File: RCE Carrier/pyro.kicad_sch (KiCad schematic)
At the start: 31 parts, among them J1 TBL002A-350-08GY-2GY, Q5 SI7232DN-T1-GE3, Q6 SI7232DN-T1-GE3, U6 LM293, U7 LM293

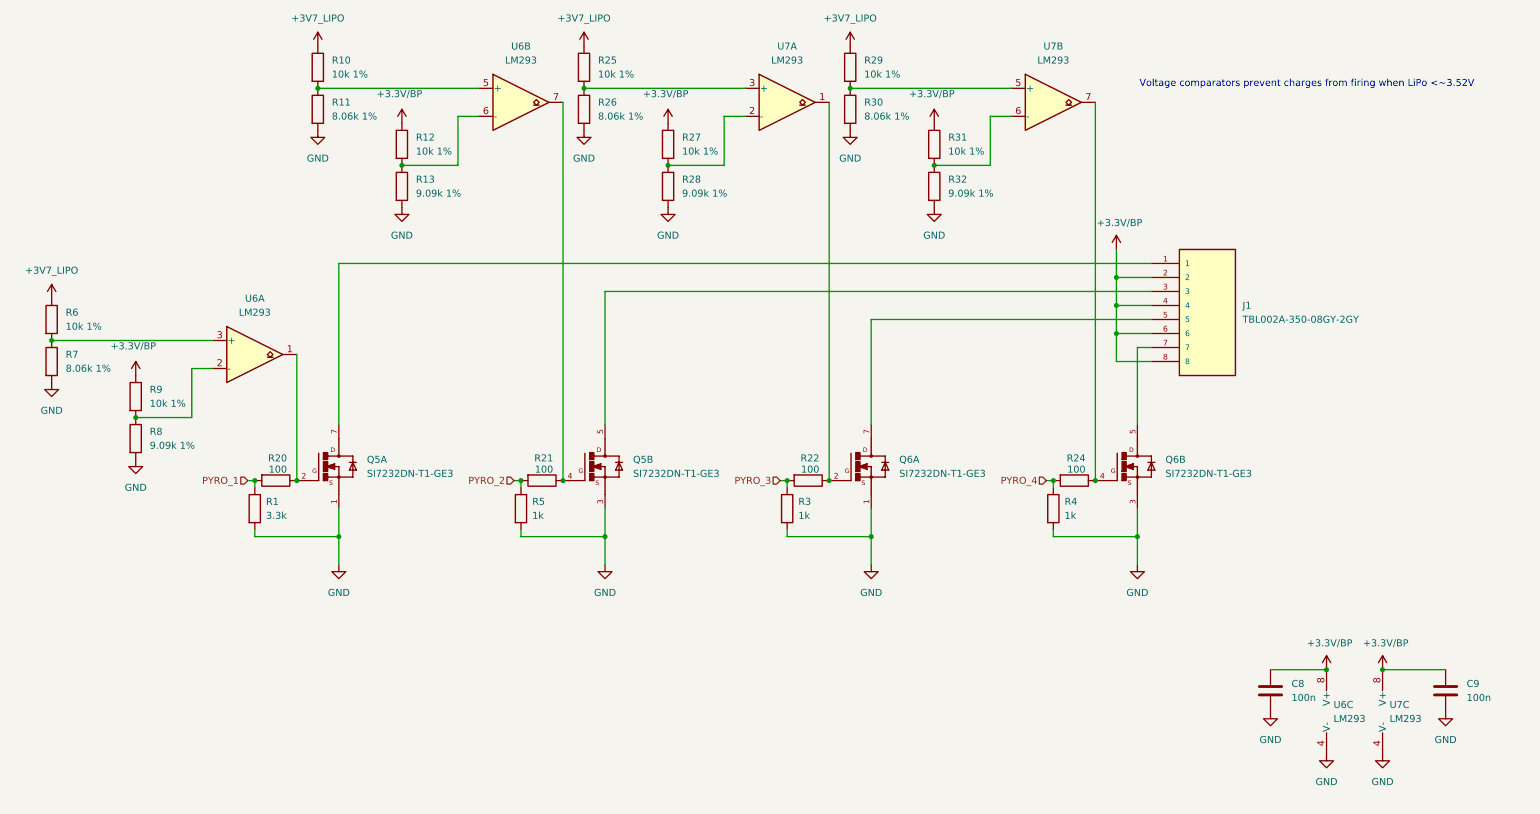
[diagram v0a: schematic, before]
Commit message: split pce and rce functions into two carriers, initial rce parts placement
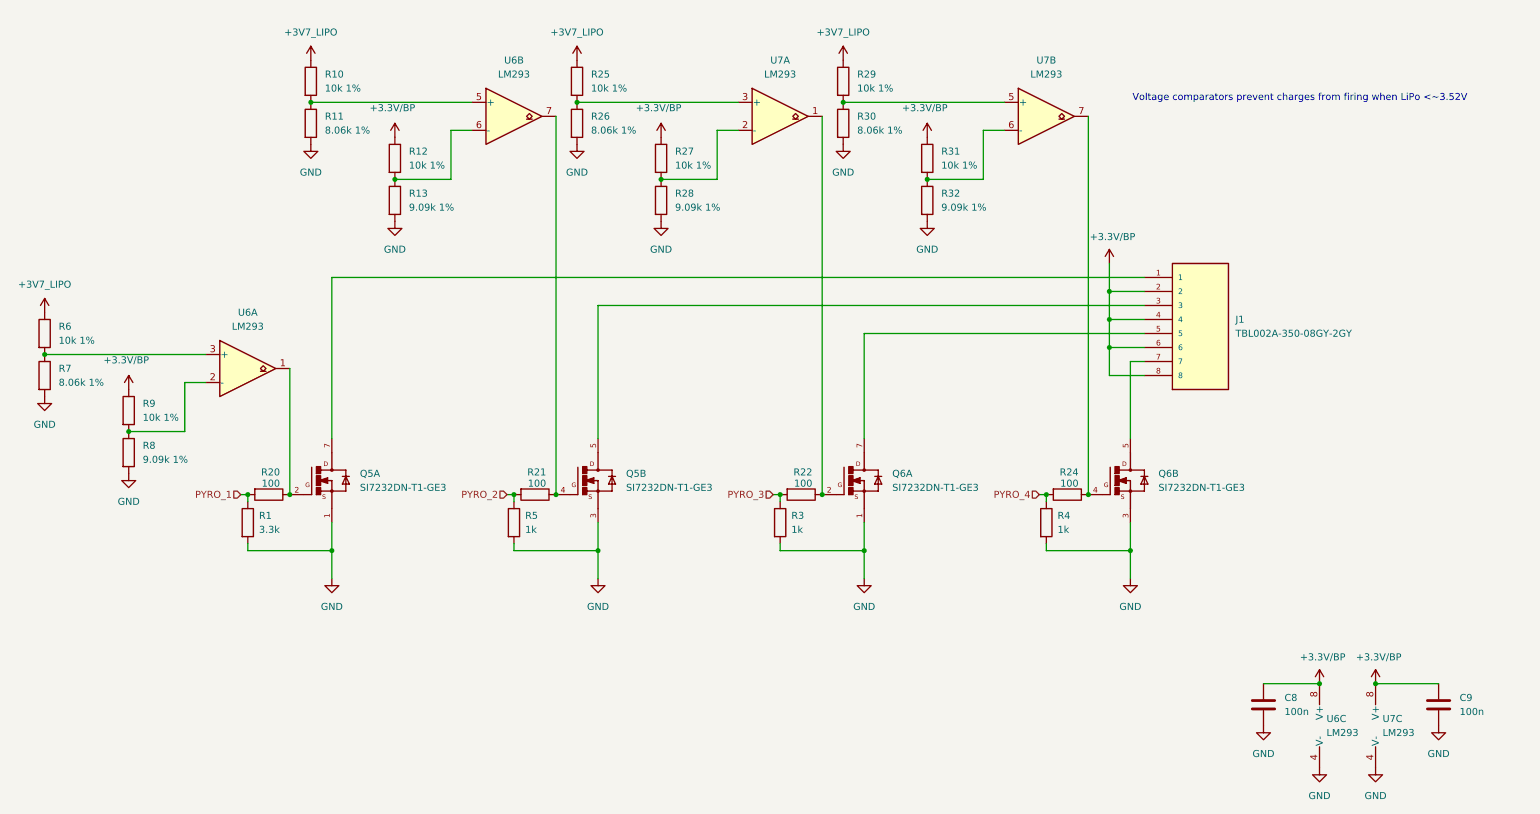
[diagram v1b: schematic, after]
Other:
- title: RCE Pyro Charges -> Airdahl Flight Computer RCE Pyro Charges

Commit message: DRC changes and updated fab files
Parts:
- R1: value 3.3k -> 1k
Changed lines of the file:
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@@
 			)
 		)
-		(property "Value" "3.3k"
+		(property "Value" "1k"
 			(at 57.912 111.76 0)
 			(show_name no)
